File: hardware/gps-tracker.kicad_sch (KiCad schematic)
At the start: 1 part

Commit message: First pass at schematic
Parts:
- removed U?: STM32G071CxU, Package_DFN_QFN:QFN-48-1EP_7x7mm_P0.5mm_EP5.6x5.6mm, symbol Homebrew:STM32G071CxU
- added C1, C14, C17, C18, C20, C24, C25, C4, C6, C8, C9: 100nF, Capacitor_SMD:C_0402_1005Metric_Pad0.74x0.62mm_HandSolder, symbol Device:C
- added C10, C11, C12, C13, C21, C22, C23, C5, C7: 10uF, Capacitor_SMD:C_0603_1608Metric, symbol Device:C
- added C15: 47uF, Capacitor_SMD:C_1206_3216Metric, symbol Device:C
- added C16, C19: 470uF, symbol Device:C_Polarized
- added C2, C3: 47pF, symbol Device:C
- added D1: SRV05-4-P-T7, Package_TO_SOT_SMD:SOT-23-6, symbol Homebrew:SRV05-4-P-T7
- added D2, D7: RED, LED_SMD:LED_0603_1608Metric, symbol Device:LED
- added D3, D4, D5: D_TVS, Diode_SMD:D_SMB, symbol Device:D_TVS
- added D6: GREEN, LED_SMD:LED_0603_1608Metric, symbol Device:LED
- added H1, H2, H3, H4: MountingHole, MountingHole:MountingHole_3.2mm_M3, symbol Mechanical:MountingHole
- added J1: USB_B_Micro, Homebrew:FRAMATOME_10118194-0001LF_fixed_bridges, symbol Connector:USB_B_Micro
- added J2: Conn_01x05, symbol Connector_Generic:Conn_01x05
- added J3: Conn_01x08, symbol Connector_Generic:Conn_01x08
- added J4: Conn_01x03, Homebrew:MiniPV_78208-X03XXX_1x03_P2.54mm_Polarized_Horizontal, symbol Connector_Generic:Conn_01x03
- added J5: Conn_01x04, Connector_PinHeader_2.54mm:PinHeader_1x04_P2.54mm_Vertical, symbol Connector_Generic:Conn_01x04
- added R1, R11, R12, R14, R18, R19, R3, R5, R7: 1k, Resistor_SMD:R_0402_1005Metric, symbol Device:R
- added R10, R13, R2, R20: 3k3, Resistor_SMD:R_0603_1608Metric, symbol Device:R
- added R15: 10k, Resistor_SMD:R_0402_1005Metric, symbol Device:R
- added R16: 62k, Resistor_SMD:R_0603_1608Metric, symbol Device:R
- added R17: 180k, Resistor_SMD:R_0603_1608Metric, symbol Device:R
- added R4, R6, R8, R9: 27, symbol Device:R
- added SW1, SW2, SW3, SW4, SW5: SW_Push, Homebrew:SW_TACTILE_5.1MM_TS-1187A-C-D-B, symbol Switch:SW_Push
- added SW6: SW_DPDT_x2, Homebrew:SK22D15L5_SP, symbol Switch:SW_DPDT_x2
- added TH1: Thermistor_PTC, Fuse:Fuse_1812_4532Metric_Pad1.30x3.40mm_HandSolder, symbol Device:Thermistor_PTC
- added U1: STM32G070KBTx, Package_QFP:LQFP-32_7x7mm_P0.8mm, symbol MCU_ST_STM32G0:STM32G070KBTx
- added U2: CH340C, Package_SO:SOIC-16_3.9x9.9mm_P1.27mm, symbol Interface_USB:CH340C
- added U3: LTR-303ALS-01, OptoDevice:Lite-On_LTR-303ALS-01, symbol Sensor_Optical:LTR-303ALS-01
- added U4: MIC5365-3.3YD5, Package_TO_SOT_SMD:SOT-23-5, symbol Regulator_Linear:MIC5365-3.3YD5
- added U5: LIS2MDLTR, Homebrew:PQFN50P200X200X70-12N, symbol Homebrew:LIS2MDLTR
- added U6: LC86LICMD, Homebrew:MODULE_LC86LICMD, symbol Homebrew:LC86LICMD
- added U7: E22-900T30S, Homebrew:XCVR_E22-900T30S, symbol Homebrew:E22-900T30S
- added U8: TP4056, Homebrew:SOP-8_3.9x4.9mm_P1.27mm_Thermal, symbol controller-rescue:TP4056-snapeda-TP4056
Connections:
- new net: J4.1 (Pin_1), TH1.2
- new net: R20.1, U8.2 (PROG)
- new net: D7.2 (A), U8.8 (CE)
- new net: D7.1 (K), R19.1
- new net: D6.1 (K), R18.1
- new net: D2.1 (K), R11.1
- new net: J2.1 (Pin_1), R14.2
- new net: R8.1, U2.2 (TXD)
- new net: R9.1, U2.3 (RXD)
- new net: R4.2, U2.5 (UD+)
- new net: R6.2, U2.6 (UD-)
- new net: J2.2 (Pin_2), R12.2
- new net: R3.2, SW3.1
- new net: R7.2, SW5.1
- new net: C18.1, U5.5 (C1)
- new net: R1.2, SW1.1
- new net: C1.2, SW2.2, U1.6 (NRST)
- new net: R5.2, SW4.1
- new net: R15.2, U4.3 (EN)
- new net +BATT: C10.2, C15.2, C19.1, C23.2, C25.1, D4.1 (A1), J2.3 (Pin_3), R15.1, R16.1, SW6.3 (C), U4.1 (VIN), U7.6 (VCC)
- new net AUX1: R12.1, U1.27 (PB3)
- new net AUX2: R14.1, U1.16 (PB1)
- new net BATT_DIRECT: C13.2, D3.1 (A1), SW6.2 (B), TH1.1, U8.5 (BAT)
- new net BOOT0: J5.4 (Pin_4), R2.1, U1.25 (PA14)
- new net COMPASS_CS: U1.1 (PB9), U5.3 (CS)
- new net GND: C10.1, C11.1, C12.1, C13.1, C14.2, C15.1, C16.2, C17.2, C18.2, C19.2, C2.2, C20.2, C21.1, C22.1, C23.1, C24.2, C25.2, C3.2, C4.1, C5.2, C6.1, C7.1, C8.2, C9.2, D1.2 (GND), D3.2 (A2), D4.2 (A2), D5.2 (A2), J1.5 (GND), J2.5 (Pin_5), J3.1 (Pin_1), J4.2 (Pin_2), J5.2 (Pin_2), R11.2, R17.2, R20.2, SW1.2, SW2.1, SW3.2, SW4.2, SW5.2, U1.5 (VSS), U2.1 (GND), U3.3 (GND), U4.2 (GND), U5.6 (GND), U5.8 (GND), U6.12 (GND), U6.3 (GND), U7.15 (GND), U7.16 (GND), U7.17 (GND), U7.7 (GND), U7.9 (GND), U8.1 (TEMP), U8.3 (GND)
- new net GPS_RXD: U1.12 (PA5), U6.1 (RXD)
- new net GPS_TXD: U1.15 (PB0), U6.2 (TXD)
- new net LED: D2.2 (A), U1.28 (PB4)
- new net MISO: U1.17 (PB2), U5.7 (INT/DRDY/SDO)
- new net MOSI: J3.6 (Pin_6), U1.11 (PA4), U5.4 (SDA/SDI/SDO)
- new net RADIO_AUX: U1.26 (PA15), U7.5 (AUX)
- new net RADIO_M0: U1.2 (PC14), U7.1 (M0)
- new net RADIO_M1: U1.3 (PC15), U7.2 (M1)
- new net RADIO_RXD: U1.30 (PB6), U7.3 (RXD)
- new net RADIO_TXD: U1.31 (PB7), U7.4 (TXD)
- new net SCK: J3.5 (Pin_5), U1.32 (PB8), U5.1 (SCL/SPC)
- new net SCL: R10.2, U1.19 (PA9/NC), U3.4 (SCL)
- new net SCREEN_BLK: J3.8 (Pin_8), U1.14 (PA7)
- new net SCREEN_CS: J3.4 (Pin_4), U1.23 (PA12/PA10)
- new net SCREEN_DC: J3.3 (Pin_3), U1.22 (PA11/PA9)
- new net SCREEN_RESETN: J3.7 (Pin_7), U1.18 (PA8)
- new net SDA: R13.2, U1.21 (PA10/NC), U3.6 (SDA)
- new net SW1: R1.1, U1.29 (PB5)
- new net SW2: R3.1, U1.7 (PA0)
- new net SW3: R5.1, U1.8 (PA1)
- new net SW4: R7.1, U1.20 (PC6)
- new net SWDIO: J5.3 (Pin_3), U1.24 (PA13)
- new net USART_RXD: R9.2, U1.9 (PA2)
- new net USART_TXD: R8.2, U1.10 (PA3)
- new net USB+: C2.1, D1.1 (IO1), J1.3 (D+), R4.1
- new net USB-: C3.1, D1.3 (IO2), J1.2 (D-), R6.1
- new net VBATT_DIV: C12.2, R16.2, R17.1, U1.13 (PA6)
- new net VBUS: C21.2, D1.5 (REF), D6.2 (A), J1.1 (VBUS), R2.2, U8.4 (VCC)
- new net VCC: C11.2, C14.1, C16.1, C17.1, C20.1, C22.2, C24.1, C4.2, C5.1, C6.2, C7.2, C8.1, C9.1, D5.1 (A1), J2.4 (Pin_4), J3.2 (Pin_2), J5.1 (Pin_1), R10.1, R13.1, U1.4 (VDD), U2.16 (VCC), U2.4 (V3), U3.1 (VDD), U4.5 (VOUT), U5.10 (VDD_IO), U5.9 (VDD), U6.4 (VCC), U6.5 (V_BCKP)
- new net ~{CHRG}: R19.2, U8.7 (~{CHRG})
- new net ~{DTR}: C1.1, U2.13 (~{DTR})
- new net ~{STDBY}: R18.2, U8.6 (~{STDBY})
- no-connect marks 0 -> 24
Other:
- note added: "150mA max"
- note added: "2A PTC"
- note added: "3k3 -> 400mA"
- note added: "650mA max (TX)"
- note added: "Compass"
- note added: "GPS"
- note added: "INPUTS"
- note added: "LDO"
- note added: "LIGHT SENSOR"
- note added: "Peak 33mA"
- note added: "RADIO"
- note added: "SCREEN"

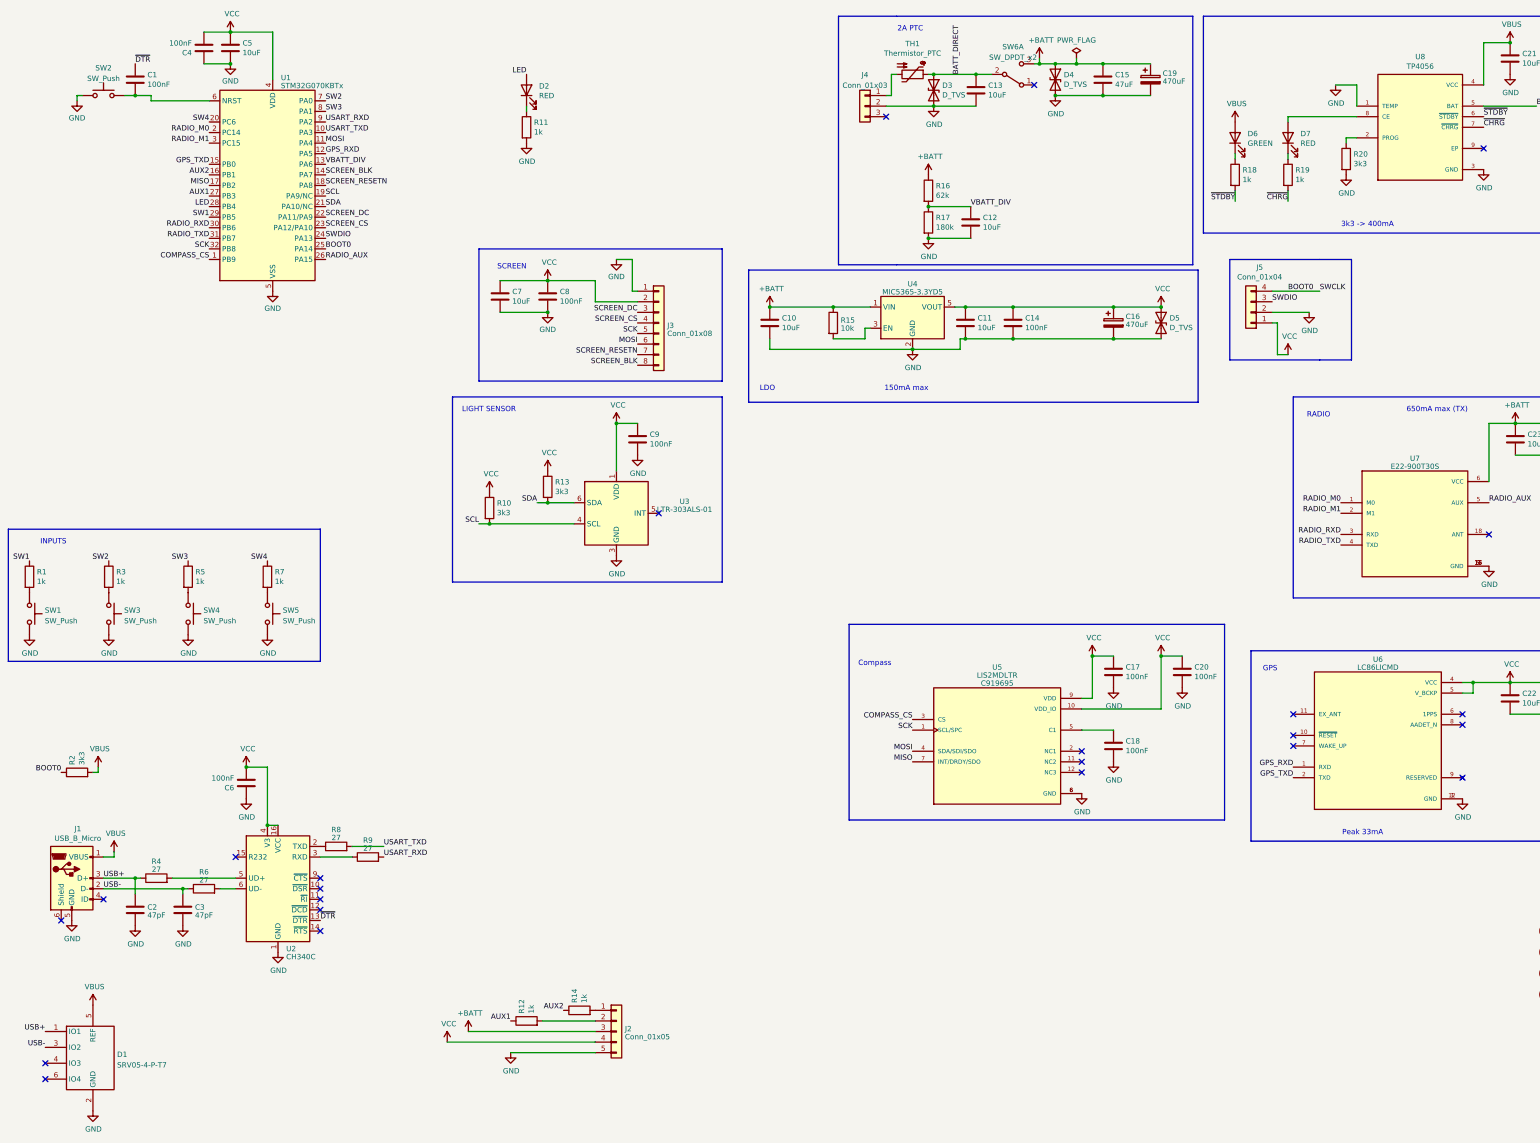
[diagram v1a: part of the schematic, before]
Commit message: Update part numbers and footprints
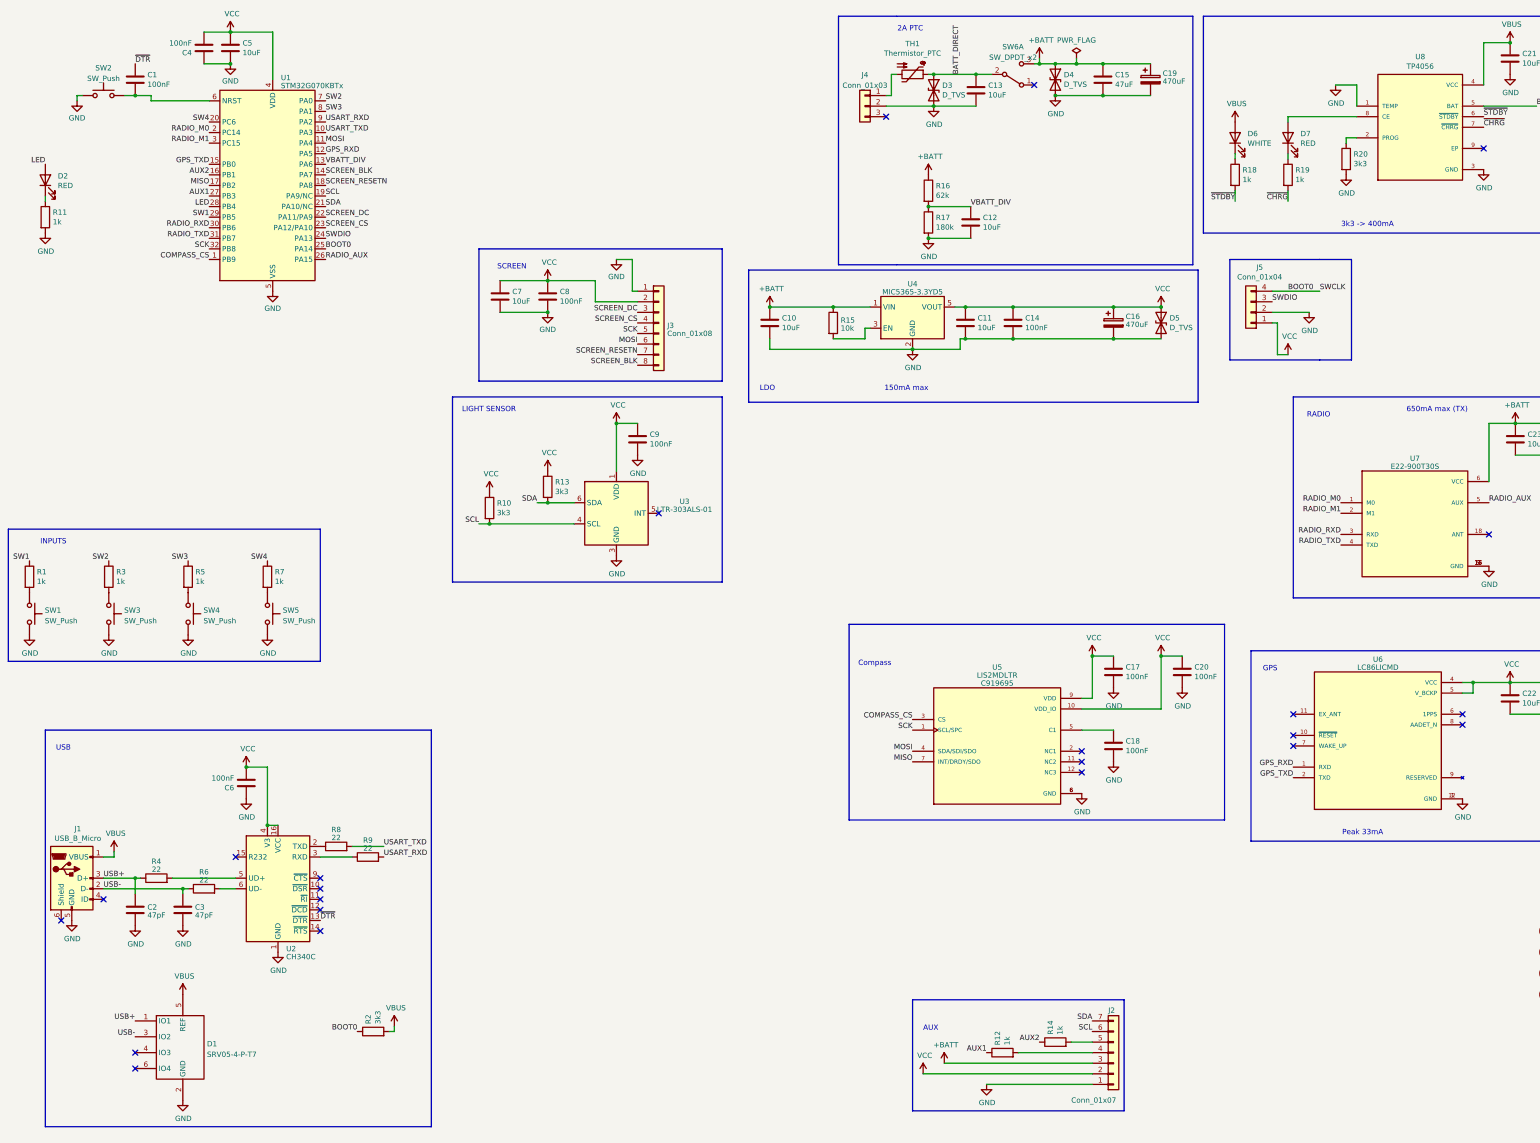
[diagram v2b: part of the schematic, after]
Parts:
- removed J2: Conn_01x05, symbol Connector_Generic:Conn_01x05
- added J2: Conn_01x07, Connector_PinHeader_2.54mm:PinHeader_1x07_P2.54mm_Vertical, symbol Connector_Generic:Conn_01x07
- C1, C14, C17, C18, C20, C24, C25, C4, C6, C8, C9: footprint Capacitor_SMD:C_0402_1005Metric_Pad0.74x0.62mm_HandSolder -> Capacitor_SMD:C_0402_1005Metric
- C16, C19: footprint (none) -> lib:CP_Radial_D6.3mm_P2.50mm; MPN (none) -> 10YXJ470M6.3X11
- C2, C3: footprint (none) -> Capacitor_SMD:C_0402_1005Metric; LCSC (none) -> C1567
- D6: value GREEN -> WHITE; LCSC (none) -> C2290; MPN LTST-C190KGKT -> (none)
- J3: footprint (none) -> Connector_PinHeader_2.54mm:PinHeader_1x08_P2.54mm_Vertical
- R15: LCSC (none) -> C25744
- R4, R6, R8, R9: value 27 -> 22; footprint (none) -> Resistor_SMD:R_0402_1005Metric; LCSC (none) -> C25092
- U1: LCSC (none) -> C529339
- U3: LCSC (none) -> C364577
- U4: MPN (none) -> MIC5365-3.3YD5
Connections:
- net +BATT: now also J2.3 (Pin_3)
- net GND: now also J2.1 (Pin_1)
- net SCL: now also J2.6 (Pin_6)
- net SDA: now also J2.7 (Pin_7)
- net VCC: now also J2.2 (Pin_2)
- net at R14.2: now also J2.5 (Pin_5)
- net at R12.2: now also J2.4 (Pin_4)
- no-connect marks 24 -> 23
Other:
- note added: "AUX"
- note added: "USB"
- moved on the sheet: D1, D2, R11, R12, R14, R2

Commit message: Update to lower-power SPI radio module
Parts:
- removed U7: E22-900T30S, Homebrew:XCVR_E22-900T30S, symbol Homebrew:E22-900T30S
- added C26, C28, C37: 47uF, Capacitor_SMD:C_1206_3216Metric, symbol Device:C
- added C27, C29, C30, C31, C32, C33, C36: 100nF, Capacitor_SMD:C_0402_1005Metric, symbol Device:C
- added C34: 10uF, Capacitor_SMD:C_0603_1608Metric, symbol Device:C
- added C38: 470uF, lib:CP_Radial_D6.3mm_P2.50mm, symbol Device:C_Polarized
- added D8: D_TVS, Diode_SMD:D_SMB, symbol Device:D_TVS
- added R21: 1k, Resistor_SMD:R_0402_1005Metric, symbol Device:R
- added R22: 10k, Resistor_SMD:R_0402_1005Metric, symbol Device:R
- added U7: E22-900M22S, Homebrew:E22-900M22S, symbol Homebrew:E22-900M22S
- added U9: MIC5365-3.3YD5, Package_TO_SOT_SMD:SOT-23-5, symbol Regulator_Linear:MIC5365-3.3YD5
- H1, H2, H3, H4, J2: now not fitted
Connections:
- net +BATT: now also C34.2, R22.1, U9.1 (VIN); no longer C23.2, C25.1
- net GND: now also C26.1, C27.2, C28.1, C29.2, C30.2, C31.2, C32.1, C33.1, C34.1, C36.2, C37.1, C38.2, D8.2 (A2), U7.1 (GND), U7.10 (GND), U7.11 (GND), U7.12 (GND), U7.2 (GND), U7.20 (GND), U7.22 (GND), U7.3 (GND), U7.4 (GND), U7.5 (GND), U9.2 (GND)
- net MISO: now also U7.16 (MISO)
- net MOSI: now also U7.17 (MOSI)
- net SCK: now also U7.18 (SCK)
- net VBUS: now also C33.2
- net VCC: now also C26.2, C29.1, C31.1, C32.2, R21.2; no longer U6.5 (V_BCKP)
- net RADIO_AUX: no longer names the net of U1.26 (PA15)
- net RADIO_M0 renamed RADIO_RXEN
- net RADIO_RXEN: now also U7.6 (RXEN)
- net RADIO_M1 renamed RADIO_CS
- net RADIO_CS: now also U7.19 (NSS)
- net RADIO_RXD renamed RADIO_DIO1
- net RADIO_DIO1: now also U7.13 (DIO1)
- net RADIO_TXD renamed RADIO_BUSY
- net RADIO_BUSY: now also U7.14 (BUSY)
- new net: C27.1, C28.2, R21.1, U6.5 (V_BCKP)
- new net: R22.2, U9.3 (EN)
- new net: U7.7 (TXEN), U7.8 (DIO2)
- new net RADIO_PWR: C23.2, C25.1, C30.1, C36.1, C37.2, C38.1, D8.1 (A1), U7.9 (VCC), U9.5 (VOUT)
- no-connect marks 23 -> 25
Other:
- note added: "V_BCKP: T = 0.047s"
- note removed: "650mA max (TX)"
- moved on the sheet: C1, C17, C18, C20, C22, C23, C24, C25, R12, R14, SW2, U5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

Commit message: First pass at PCB positions
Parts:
- removed H4: MountingHole, MountingHole:MountingHole_3.2mm_M3, symbol Mechanical:MountingHole
- removed SW6: SW_DPDT_x2, Homebrew:SK22D15L5_SP, symbol Switch:SW_DPDT_x2
- added C35: 10uF, Capacitor_SMD:C_0603_1608Metric, symbol Device:C
- added R23, R24: 220, Resistor_SMD:R_0402_1005Metric, symbol Device:R
- added R25: 1k, Resistor_SMD:R_0402_1005Metric, symbol Device:R
- added SW6: SW_SPDT, Homebrew:SS-12D03-G5, symbol Switch:SW_SPDT
- C16, C19, C38: footprint lib:CP_Radial_D6.3mm_P2.50mm -> Homebrew:CP_Radial_D6.3mm_P2.50mm_470uF
- D3, D4, D5, D8: footprint Diode_SMD:D_SMB -> Diode_SMD:D_SOD-123F; LCSC C78395 -> C2990473
- R12, R14, R21: footprint Resistor_SMD:R_0402_1005Metric -> Resistor_SMD:R_0603_1608Metric; LCSC C11702 -> C21190
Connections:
- net +BATT: now also SW6.2 (B)
- net BATT_DIRECT: now also SW6.1 (A)
- net GND: now also C35.1
- net RADIO_RXEN: now also R23.1; no longer U7.6 (RXEN)
- net VCC: now also C35.2
- net at U7.7 (TXEN): now also R24.1; no longer U7.8 (DIO2)
- net at C1.2, U1.6 (NRST): now also R25.2; no longer SW2.2
- new net: R24.2, U7.8 (DIO2)
- new net: R23.2, U7.6 (RXEN)
- new net: R25.1, SW2.2
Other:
- moved on the sheet: C1, C20

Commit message: Hardware v1.0
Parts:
- removed C13: 10uF, Capacitor_SMD:C_0603_1608Metric, symbol Device:C
- removed C3: 47pF, Capacitor_SMD:C_0402_1005Metric, symbol Device:C
- removed C38: 470uF, Homebrew:CP_Radial_D6.3mm_P2.50mm_470uF, symbol Device:C_Polarized
- removed R9: 22, Resistor_SMD:R_0402_1005Metric, symbol Device:R
- removed U2: CH340C, Package_SO:SOIC-16_3.9x9.9mm_P1.27mm, symbol Interface_USB:CH340C
- added C3: 220uF, Capacitor_THT:CP_Radial_D10.0mm_P5.00mm, symbol Device:C_Polarized
- added D9: D, Diode_SMD:D_SMA, symbol Device:D
- added J6: Conn_01x03, Connector_PinHeader_2.54mm:PinHeader_1x03_P2.54mm_Vertical, symbol Connector_Generic:Conn_01x03
- added J7: Conn_01x02, Homebrew:JST_Micro_1x02_P1.25mm_Horizontal, symbol Connector_Generic:Conn_01x02
- added U2: CH340X, Package_SO:MSOP-10_3x3mm_P0.5mm, symbol Interface_USB:CH340E
- C16, C19: value 470uF -> 220uF; footprint Homebrew:CP_Radial_D6.3mm_P2.50mm_470uF -> Capacitor_THT:CP_Radial_D10.0mm_P5.00mm; MPN 10YXJ470M6.3X11 -> ER1E221MP51007RU
- C2: value 47pF -> 10uF; footprint Capacitor_SMD:C_0402_1005Metric -> Capacitor_SMD:C_0603_1608Metric; LCSC C1567 -> C96446
- R2: value 3k3 -> 220; footprint Resistor_SMD:R_0603_1608Metric -> Resistor_SMD:R_0402_1005Metric; LCSC C22978 -> C25091
- R4: value 22 -> 4k7; LCSC C25092 -> C25900
- R6: value 22 -> 1k; LCSC C25092 -> C11702
- R8: value 22 -> 220; LCSC C25092 -> C25091
- TH1: footprint Fuse:Fuse_1812_4532Metric_Pad1.30x3.40mm_HandSolder -> Fuse:Fuse_0805_2012Metric; LCSC C89650 -> C269104
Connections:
- net +BATT: now also C16.1; no longer C19.1
- net BATT_DIRECT: now also C2.2, SW6.3 (C), D9.1 (K), J6.3 (Pin_3); no longer SW6.1 (A)
- net BOOT0: now also U2.4 (~{RTS}); no longer R2.1
- net GND: now also C2.1, C3.2, D9.2 (A), J7.1 (Pin_1), U2.3 (GND); no longer C2.2
- net RADIO_CS: now also U1.26 (PA15); no longer U1.3 (PC15)
- net RADIO_PWR: now also C3.1
- net RADIO_RXEN: now also U1.20 (PC6); no longer U1.2 (PC14)
- net SW1: now also U1.7 (PA0); no longer U1.29 (PB5)
- net SW2: now also U1.29 (PB5); no longer U1.7 (PA0)
- net SW4: now also U1.2 (PC14); no longer U1.20 (PC6)
- net USB+: now also U2.1 (UD+); no longer C2.1, R4.1
- net USB-: now also U2.2 (UD-); no longer R6.1
- net VBUS: now also D7.2 (A), R6.1; no longer R2.2
- net VCC: now also C19.1, J6.1 (Pin_1), U2.10 (V3), U2.7 (VCC); no longer C16.1, R21.2
- net ~{DTR}: now also R4.2, U2.6 (TNOW)
- net at J4.1 (Pin_1), TH1.2: now also J7.2 (Pin_2)
- net at U8.8 (CE): now also R6.2; no longer D7.2 (A)
- net at R8.1: now also U2.8 (TXD)
- net GPS_RXD renamed GPS_TX
- net GPS_TXD renamed GPS_RX
- net USART_RXD renamed USART_TX
- net USART_TX: now also R2.2
- net USART_TXD renamed USART_RX
- new net: R2.1, U2.9 (RXD)
- new net: J6.2 (Pin_2), R21.2
- new net: R4.1, U2.5 (~{CTS})
- no-connect marks 25 -> 19
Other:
- note added: "500mA PTC"
- note removed: "2A PTC"
- moved on the sheet: C22, C24, C29, C31, C6, D1, D3, J4, R8, SW6, TH1
